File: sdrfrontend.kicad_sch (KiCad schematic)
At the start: 7 parts, among them U1 CD4066BE

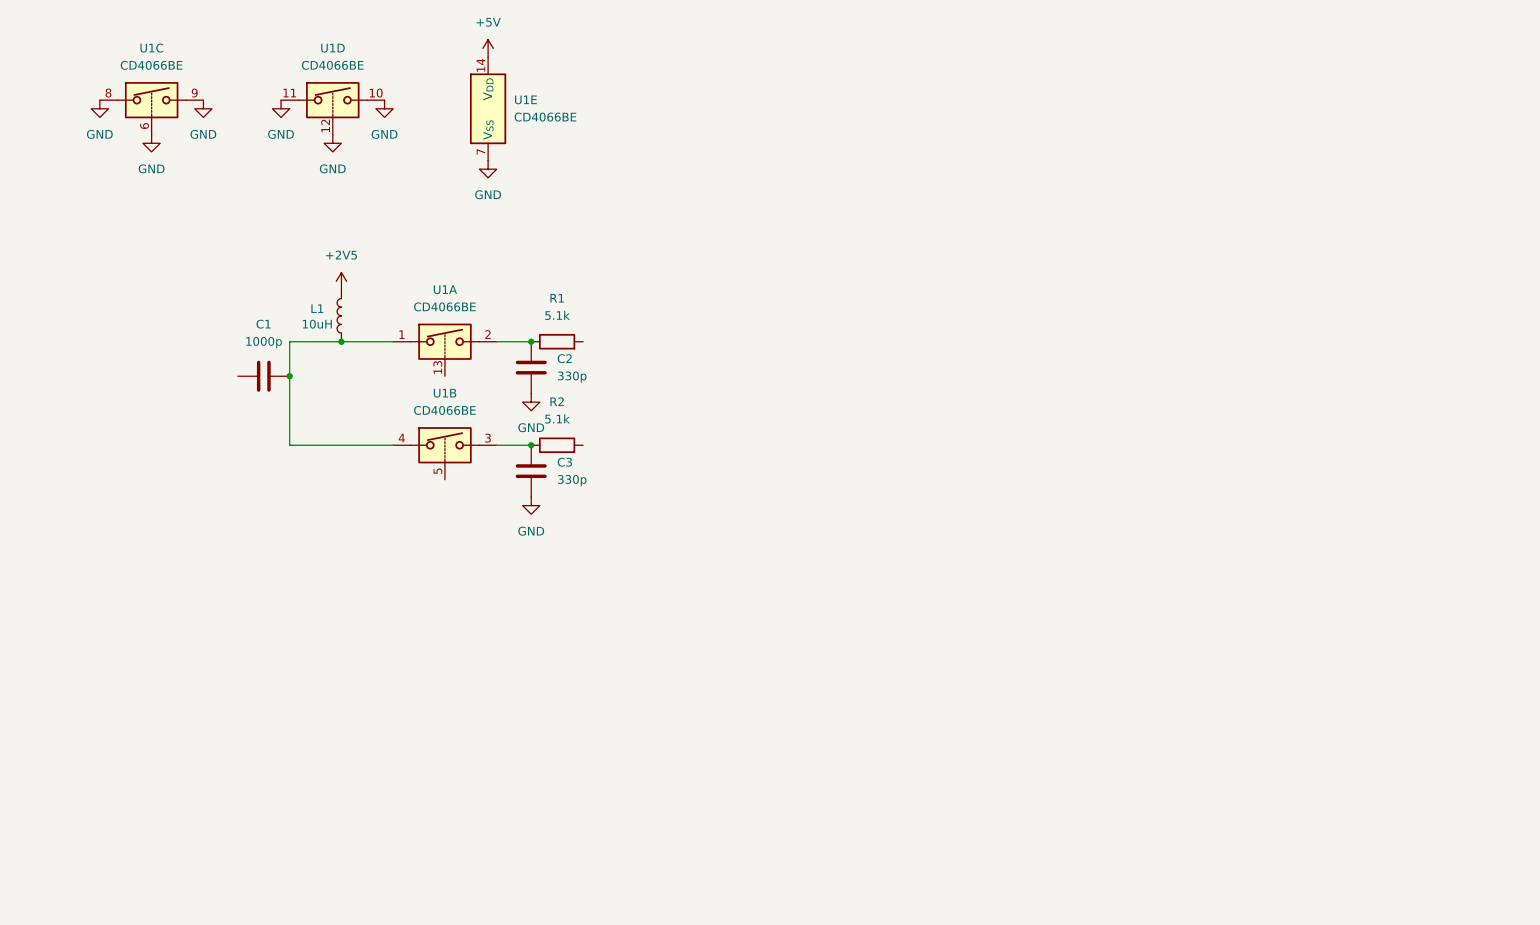
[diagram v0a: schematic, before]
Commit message: wiring parts
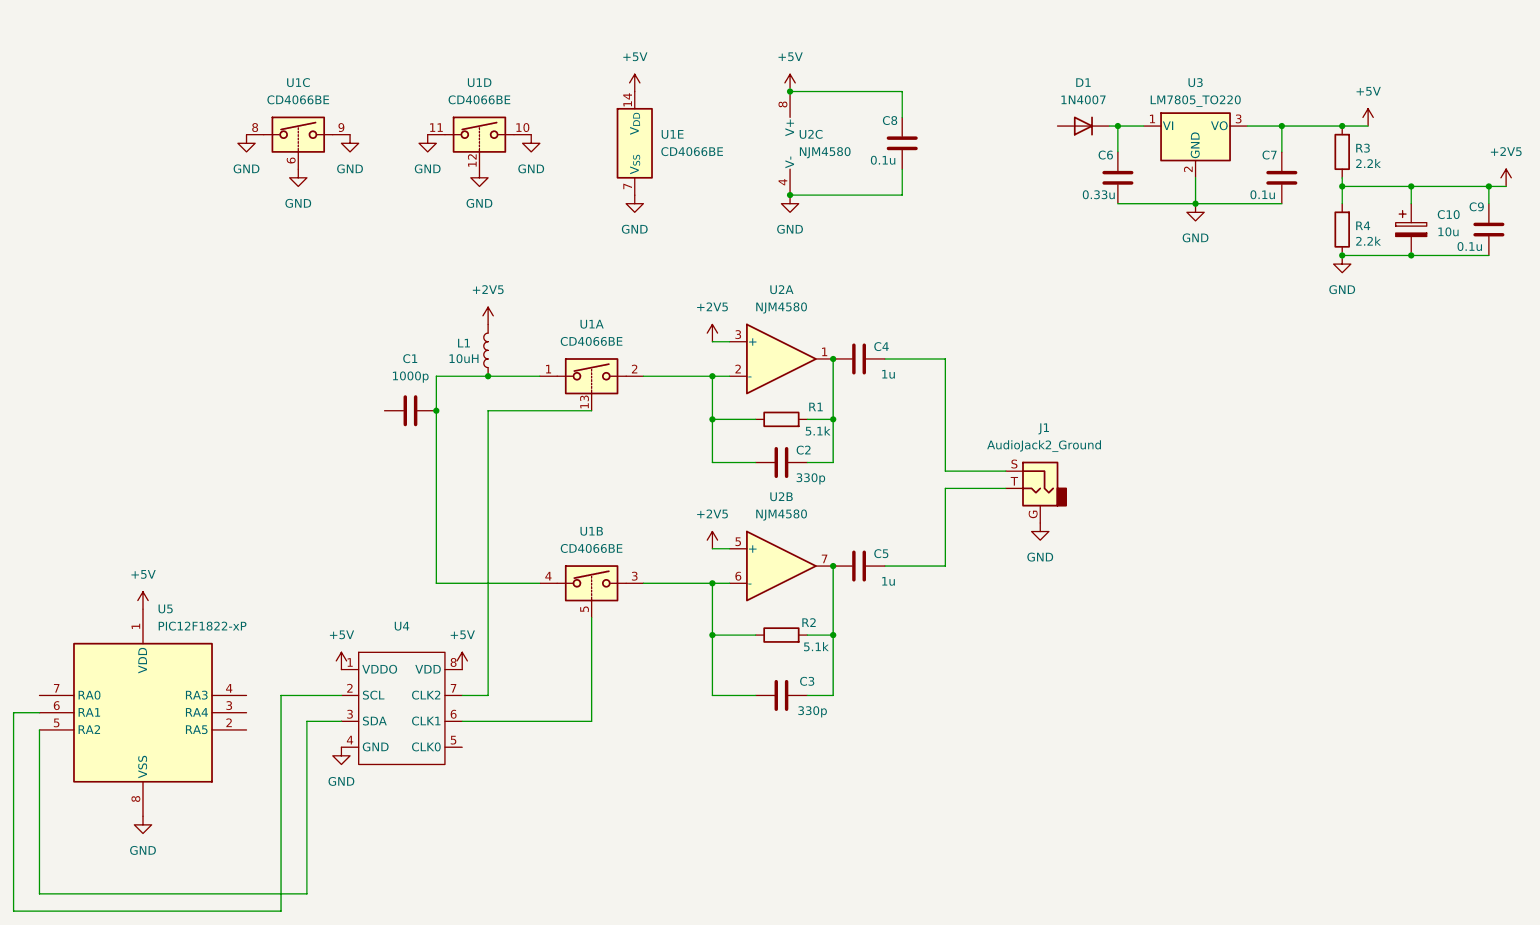
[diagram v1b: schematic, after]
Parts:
- added C10: 10u, Capacitor_THT:CP_Radial_D5.0mm_P2.50mm, symbol Device:C_Polarized
- added C4, C5: 1u, Capacitor_THT:C_Disc_D3.0mm_W1.6mm_P2.50mm, symbol Device:C
- added C6: 0.33u, Capacitor_THT:C_Disc_D3.0mm_W1.6mm_P2.50mm, symbol Device:C
- added C7, C8, C9: 0.1u, Capacitor_THT:C_Disc_D3.0mm_W1.6mm_P2.50mm, symbol Device:C
- added D1: 1N4007, Diode_THT:D_A-405_P7.62mm_Horizontal, symbol Device:D
- added J1: AudioJack2_Ground, Library:2.5jack, symbol Connector_Audio:AudioJack2_Ground
- added R3, R4: 2.2k, Resistor_THT:R_Axial_DIN0207_L6.3mm_D2.5mm_P7.62mm_Horizontal, symbol Device:R
- added U2: NJM4580, Package_DIP:DIP-8_W7.62mm, symbol Amplifier_Operational:NJM4580
- added U3: LM7805_TO220, Package_TO_SOT_THT:TO-220-3_Vertical, symbol Regulator_Linear:LM7805_TO220
- added U4: ~, Package_DIP:DIP-8_W7.62mm, symbol New_Library:si5351
- added U5: PIC12F1822-xP, Package_DIP:DIP-8_W7.62mm, symbol MCU_Microchip_PIC12:PIC12F1822-xP
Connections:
- net +2V5: now also C10.1, C9.1, R3.1, R4.2, U2.3 (+), U2.5 (+)
- net +5V: now also C7.1, C8.1, R3.2, U2.8 (V+), U3.3 (VO), U4.1 (VDDO), U4.8 (VDD), U5.1 (VDD)
- net GND: now also C10.2, C6.2, C7.2, C8.2, C9.2, J1.G, R4.1, U2.4 (V-), U3.2 (GND), U4.4 (GND), U5.8 (VSS); no longer C2.1, C3.1
- net at C3.2, R2.1, U1.3: now also U2.6 (-)
- net at R2.2: now also C3.1, C5.2, U2.7
- net at C2.2, R1.1, U1.2: now also U2.2 (-)
- net at U1.13: now also U4.7 (CLK2)
- net at U1.5: now also U4.6 (CLK1)
- net at R1.2: now also C2.1, C4.2, U2.1
- new net: U4.2 (SCL), U5.6 (RA1)
- new net: U4.3 (SDA), U5.5 (RA2)
- new net: C5.1, J1.T
- new net: C4.1, J1.S
- new net: C6.1, D1.1 (K), U3.1 (VI)
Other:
- moved on the sheet: C1, C2, C3, L1, R1, R2, U1A, U1B, U1C, U1D, U1E

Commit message: make pcb
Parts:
- R1, R2: footprint Resistor_THT:R_Axial_DIN0207_L6.3mm_D2.5mm_P7.62mm_Horizontal -> Resistor_THT:R_Axial_DIN0207_L6.3mm_D2.5mm_P2.54mm_Vertical
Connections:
- net GND: now also U1.1, U1.13, U1.2; no longer U1.6, U1.8, U1.9
- net at C3.2, R2.1, U1.3: now also U2.2 (-); no longer U2.6 (-)
- net at C3.1, R2.2: now also C4.2, U2.1; no longer C5.2, U2.7
- net at C2.1, R1.2: now also C5.2, U2.7; no longer C4.2, U2.1
- net at C2.2, R1.1: now also U1.9, U2.6 (-); no longer U1.2, U2.2 (-)
- net at U4.6 (CLK1): now also U1.6; no longer U1.5
- net at U4.7 (CLK2): now also U1.5; no longer U1.13
- net at C1.2, L1.1, U1.4: now also U1.8; no longer U1.1
- net at C5.1: now also J1.S; no longer J1.T
- net at C4.1: now also J1.T; no longer J1.S
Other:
- moved on the sheet: C2, C3, R1, R2

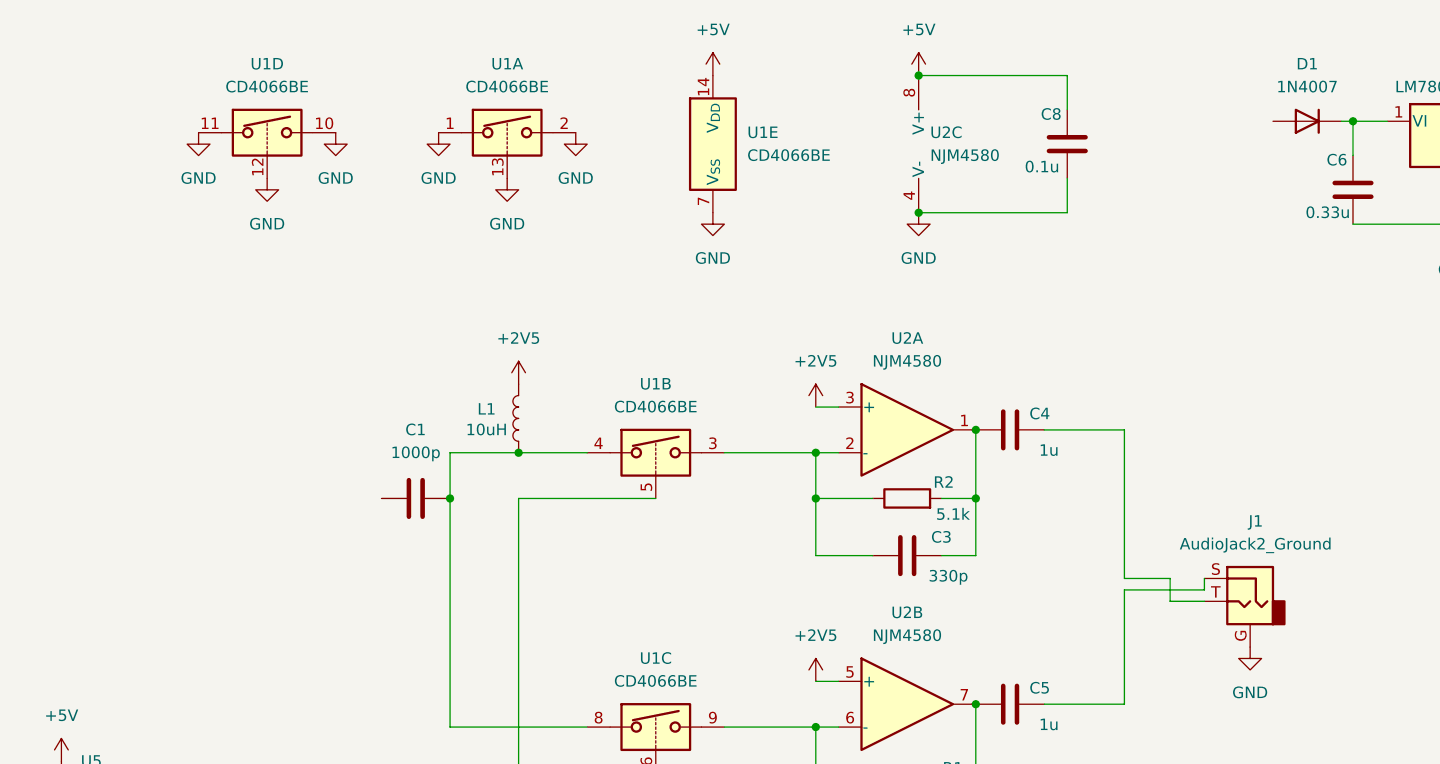
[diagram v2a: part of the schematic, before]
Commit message: add switch and sma conn
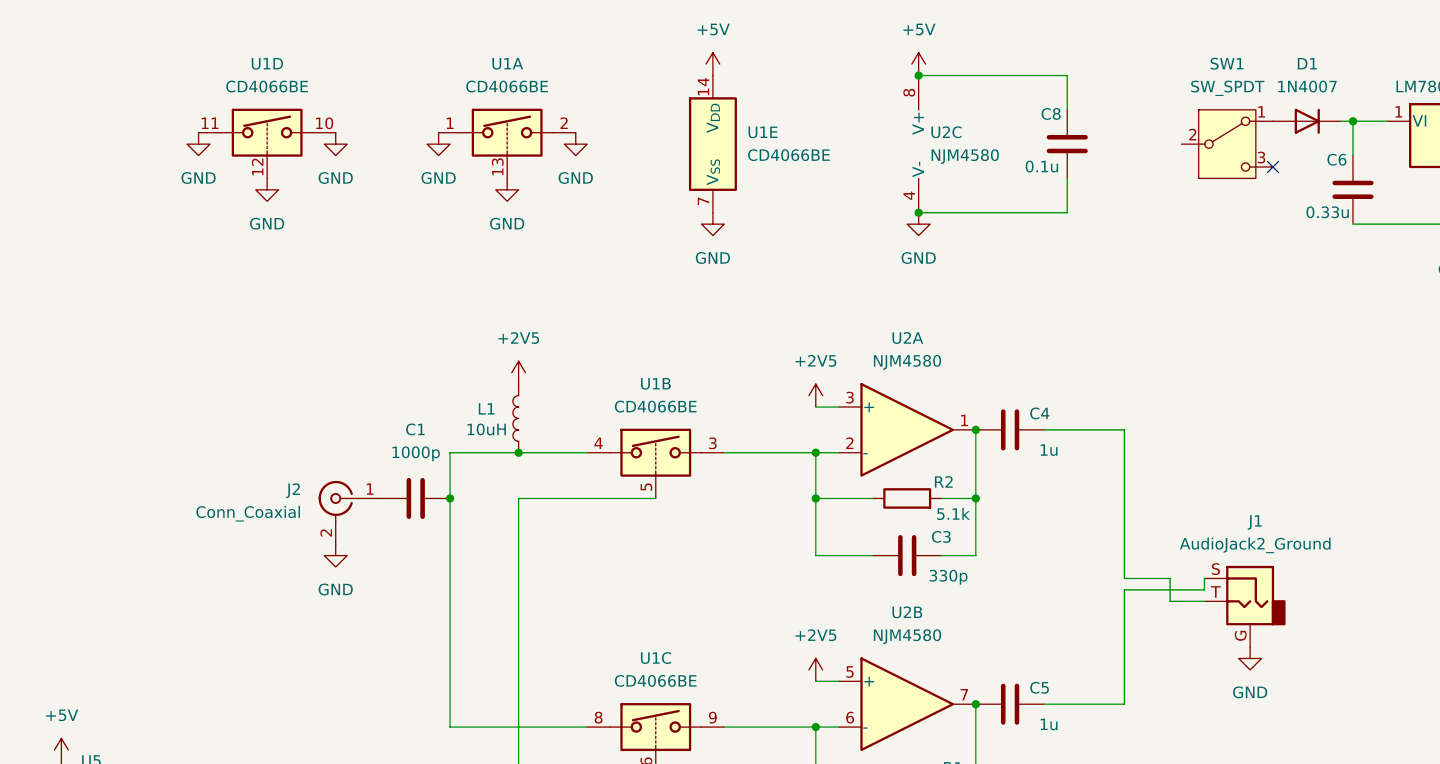
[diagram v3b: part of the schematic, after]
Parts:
- added J2: Conn_Coaxial, Connector_Coaxial:SMA_Amphenol_132289_EdgeMount, symbol Connector:Conn_Coaxial
- added SW1: SW_SPDT, Button_Switch_THT:SW_Slide-03_Wuerth-WS-SLTV_10x2.5x6.4_P2.54mm, symbol Switch:SW_SPDT
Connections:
- net GND: now also J2.2 (Ext)
- net at D1.2 (A): now also SW1.1 (A)
- net at C1.1: now also J2.1 (In)
- no-connect marks 0 -> 1
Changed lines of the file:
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@@
 		(color 0 0 0 0)
 	)
+	(no_connect
+		(at 173.99 34.29)
+	)
 	(wire
 		(pts
@@
 	)
 	(symbol
+		(lib_id "Switch:SW_SPDT")
+		(at 168.91 31.75 0)
+		(unit 1)
+		(exclude_from_sim no)
+		(in_bom yes)
+		(on_board yes)
+		(dnp no)
+		(fields_autoplaced yes)
+		(property "Reference" "SW1"
+			(at 168.91 22.86 0)
+			(effects
+				(font
+					(size 1.27 1.27)
+				)
+			)
+		)
+		(property "Value" "SW_SPDT"
+			(at 168.91 25.4 0)
+			(effects
+				(font
+					(size 1.27 1.27)
+				)
+			)
+		)
+		(property "Footprint" "Button_Switch_THT:SW_Slide-03_Wuerth-WS-SLTV_10x2.5x6.4_P2.54mm"
+			(at 168.91 31.75 0)
+			(effects
+				(font
+					(size 1.27 1.27)
+				)
+				(hide yes)
+			)
+		)
+		(property "Datasheet" "~"
+			(at 168.91 39.37 0)
+			(effects
+				(font
+					(size 1.27 1.27)
+				)
+				(hide yes)
+			)
+		)
+		(property "Description" "Switch, single pole double throw"
+			(at 168.91 31.75 0)
+			(effects
+				(font
+					(size 1.27 1.27)
+				)
+				(hide yes)
+			)
+		)
+		(pin "3"
+		)
+		(pin "1"
+		)
+		(pin "2"
+		)
+		(instances
+			(project ""
+				(path "/5a5e6f87-7ce6-4b7b-92a6-5808dc0ec353"
+					(reference "SW1")
+					(unit 1)
+				)
+			)
+		)
+	)
+	(symbol
 		(lib_id "New_Library:si5351")
 		(at 77.47 115.57 0)
@@
 	)
 	(symbol
+		(lib_id "power:GND")
+		(at 69.85 76.2 0)
+		(unit 1)
+		(exclude_from_sim no)
+		(in_bom yes)
+		(on_board yes)
+		(dnp no)
+		(fields_autoplaced yes)
+		(property "Reference" "#PWR024"
+			(at 69.85 82.55 0)
+			(effects
+				(font
+					(size 1.27 1.27)
+				)
+				(hide yes)
+			)
+		)
+		(property "Value" "GND"
+			(at 69.85 81.28 0)
+			(effects
+				(font
+					(size 1.27 1.27)
+				)
+			)
+		)
+		(property "Footprint" ""
+			(at 69.85 76.2 0)
+			(effects
+				(font
+					(size 1.27 1.27)
+				)
+				(hide yes)
+			)
+		)
+		(property "Datasheet" ""
+			(at 69.85 76.2 0)
+			(effects
+				(font
+					(size 1.27 1.27)
+				)
+				(hide yes)
+			)
+		)
+		(property "Description" "Power symbol creates a global label with name \"GND\" , ground"
+			(at 69.85 76.2 0)
+			(effects
+				(font
+					(size 1.27 1.27)
+				)
+				(hide yes)
+			)
+		)
+		(pin "1"
+		)
+		(instances
+			(project "sdrfrontend"
+				(path "/5a5e6f87-7ce6-4b7b-92a6-5808dc0ec353"
+					(reference "#PWR024")
+					(unit 1)
+				)
+			)
+		)
+	)
+	(symbol
 		(lib_id "Device:C")
 		(at 207.01 36.83 0)
@@
 	)
 	(symbol
+		(lib_id "Connector:Conn_Coaxial")
+		(at 69.85 71.12 0)
+		(mirror y)
+		(unit 1)
+		(exclude_from_sim no)
+		(in_bom yes)
+		(on_board yes)
+		(dnp no)
+		(property "Reference" "J2"
+			(at 66.04 70.1431 0)
+			(effects
+				(font
+					(size 1.27 1.27)
+				)
+				(justify left)
+			)
+		)
+		(property "Value" "Conn_Coaxial"
+			(at 66.04 72.6831 0)
+			(effects
+				(font
+					(size 1.27 1.27)
+				)
+				(justify left)
+			)
+		)
+		(property "Footprint" "Connector_Coaxial:SMA_Amphenol_132289_EdgeMount"
+			(at 69.85 71.12 0)
+			(effects
+				(font
+					(size 1.27 1.27)
+				)
+				(hide yes)
+			)
+		)
+		(property "Datasheet" "~"
+			(at 69.85 71.12 0)
+			(effects
+				(font
+					(size 1.27 1.27)
+				)
+				(hide yes)
+			)
+		)
+		(property "Description" "coaxial connector (BNC, SMA, SMB, SMC, Cinch/RCA, LEMO, ...)"
+			(at 69.85 71.12 0)
+			(effects
+				(font
+					(size 1.27 1.27)
+				)
+				(hide yes)
+			)
+		)
+		(pin "1"
+		)
+		(pin "2"
+		)
+		(instances
+			(project ""
+				(path "/5a5e6f87-7ce6-4b7b-92a6-5808dc0ec353"
+					(reference "J2")
+					(unit 1)
+				)
+			)
+		)
+	)
+	(symbol
 		(lib_id "power:+2V5")
 		(at 240.03 38.1 0)
@@
 		)
 		(instances
-			(project ""
+			(project "sdrfrontend"
 				(path "/5a5e6f87-7ce6-4b7b-92a6-5808dc0ec353"
 					(reference "#PWR02")
